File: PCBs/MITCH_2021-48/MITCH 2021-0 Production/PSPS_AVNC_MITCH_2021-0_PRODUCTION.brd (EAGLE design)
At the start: 25.4 x 58.1 mm, 58 parts, among them J1 A-1JB, J2 TFM-107-01-XXX-D-DS, U0-C STM32F411CEUX, U1-S ICM-20948, U11-S SN74LV1T34, U12-S SN74LV1T34, U13-S SN74LV1T34, U14-S SN74LV1T34, U14-S1 SN74LV1T34, U14-S2 SN74LV1T34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

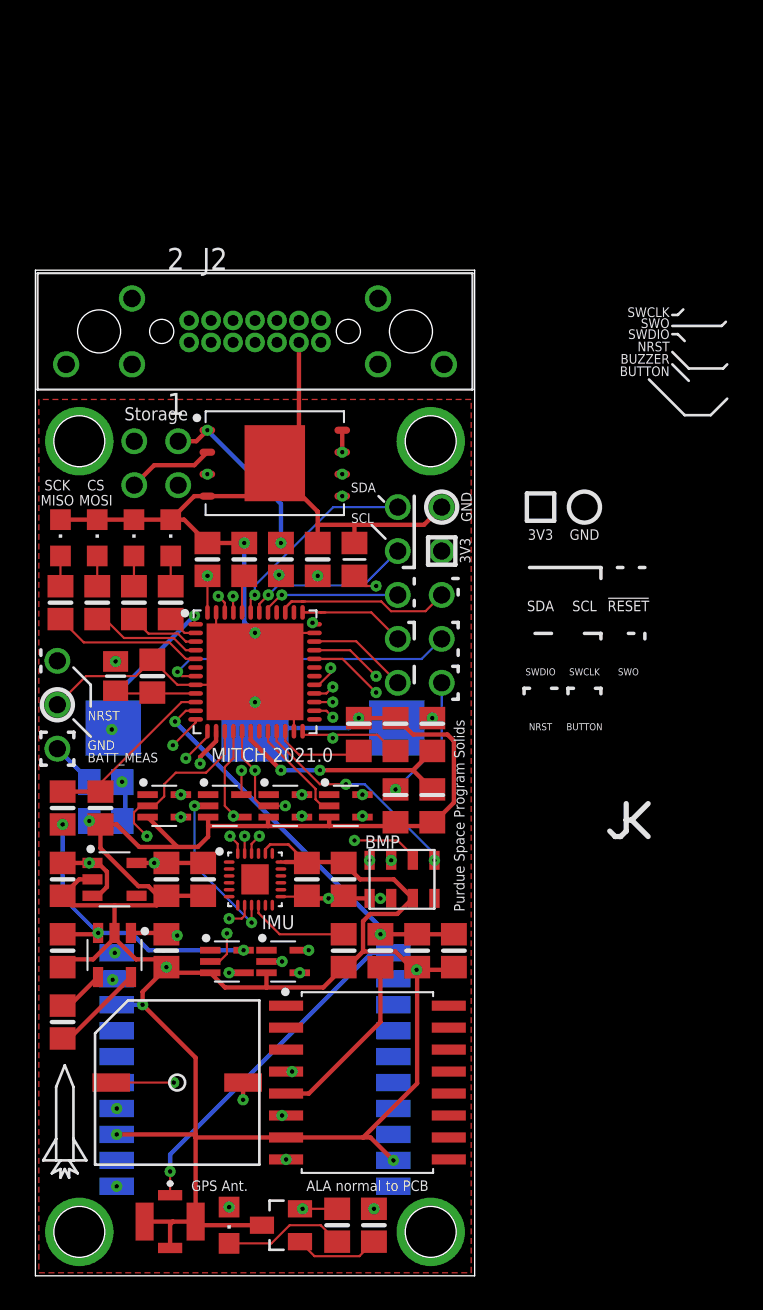
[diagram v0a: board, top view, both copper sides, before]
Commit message: Improved Battery board interface nets
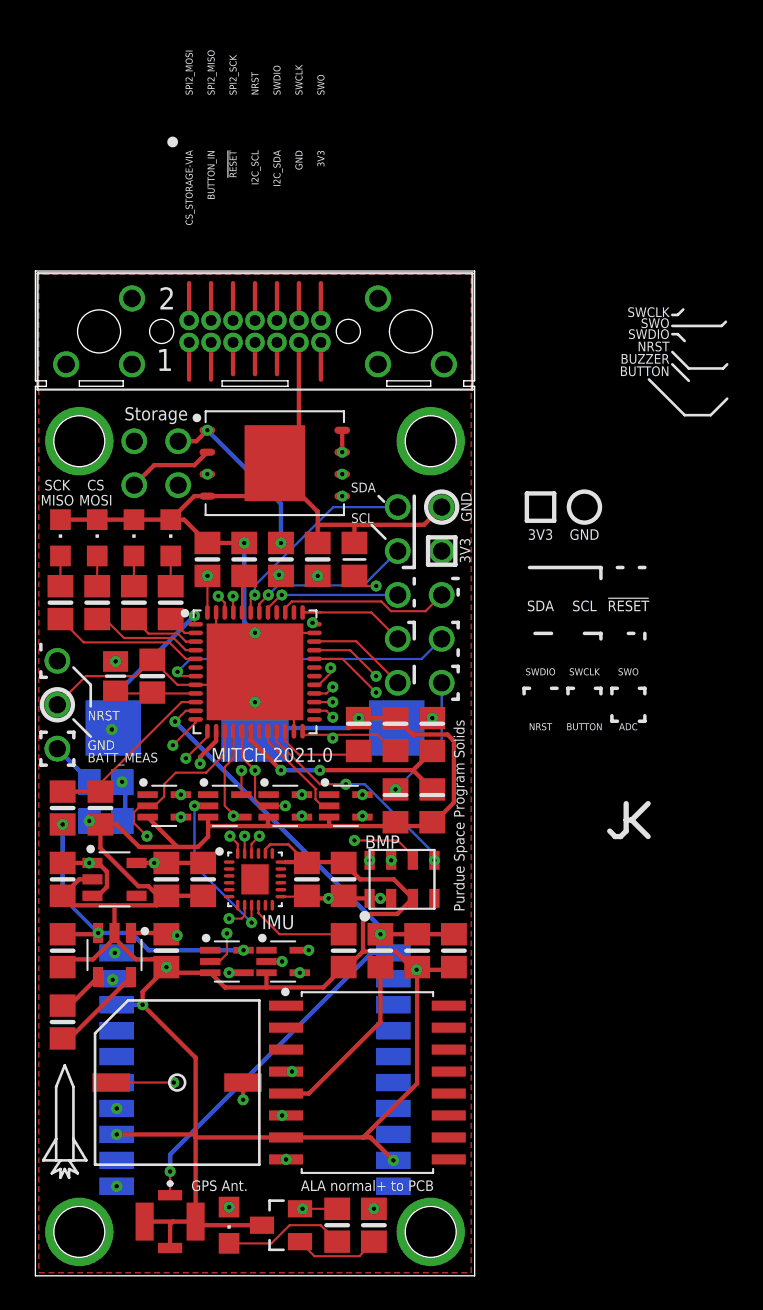
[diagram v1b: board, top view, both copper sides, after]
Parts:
- R2: value (none) -> 10k
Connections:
- net GND: now also J2.15, J2.16, J2.17, J2.18, J2.19, J2.20
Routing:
- net BUTTON_IN: track 40.6 -> 44.6 mm
- net GND: track 249.3 -> 245.5 mm
- net I2C_SCL: track 25.6 -> 29.3 mm
- net I2C_SDA: track 24.2 -> 27.8 mm
- net !RESET!: track 27.8 -> 31.2 mm
- net SPI2_SCK: track 43.3 -> 45.4 mm
- net SPI2_MOSI: track 35.4 -> 37.5 mm
- net SPI2_MISO: track 39.5 -> 41.7 mm
- net CS_STORAGE-VIA: track 15.7 -> 17.9 mm
- net SWO: track 33.3 -> 35.3 mm
- net SWDIO: track 39.5 -> 41.3 mm
- net SWCLK: track 35.9 -> 37.7 mm
- net 5V: track 34.2 -> 32.9 mm
- net N$15: track 21.1 -> 20.1 mm
- net 3V3: track 161.2 -> 162.0 mm
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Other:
- outline, holes or cut-outs redrawn
- board text added: "ADC"
- board text added: "ALA normal+ to PCB"
- board text added: "BUTTON_IN"
- board text added: "CS_STORAGE-VIA"
- board text added: "I2C_SCL"
- board text added: "I2C_SDA"
- board text added: "Removable External Connector"
- board text added: "SPI2_MISO"
- board text added: "SPI2_MOSI"
- board text added: "SPI2_SCK"
- board text removed: "ALA normal to PCB"
